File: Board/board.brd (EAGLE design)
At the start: 172.4 x 118.1 mm, 13 parts, among them IC1 L297, IC2 MEGA32-P, J1 +12V

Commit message: Fan, water pump, and supply for motor drive eagle
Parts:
- added C5, C6: 100nF, rcl:C025-025X050
- added C7: 10uF, resistor:E5-10,5
- added D2, D3: 1N5824, diode:DO41-7.6
- added Q1, Q2: BC639, transistor-small-signal:SOT54D
- added R1, R3: (no value), rcl:0207/12
- added R2: 10K, rcl:0207/12
- added S1: (no value), switch-omron:B3F-10XX
- added X1: WATER_PUMP, con-ptr500:AK500/2
- added X2: FAN, con-ptr500:AK500/3
- added X3: STEP_MOT_CD, con-ptr500:AK500/2
- added X4: STEP_MOT_AB, con-ptr500:AK500/2
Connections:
- removed net N$4 (its old number): IC2.9, KANDA.5
- new net N$10: C5.1, IC2.9, KANDA.5, R2.1, S1.1, S1.2
- new net N$11: D3.C, Q2.E, X1.2
- new net N$12: IC2.21, R3.1
- new net N$13: IC1.9, X3.1
- new net N$14: IC1.7, X3.2
- new net N$15: IC1.6, X4.1
- new net N$16: IC1.4, X4.2
- new net N$5: D2.C, Q1.E, X2.3
- new net N$7: Q2.B, R3.2
- new net N$8: Q1.B, R1.2
- new net N$9: IC2.4, R1.1
- new net OLED_RST: IC2.25, OLED_SSD3306_CON.8
- new net OLED_SA: IC2.24, OLED_SSD3306_CON.7
- new net SCL: IC2.22, OLED_SSD3306_CON.5
- new net SDA: IC2.23, OLED_SSD3306_CON.4
- net GND: now also C5.2, C6.2, C7.-, D2.A, D3.A, IC1.11, IC1.13, IC1.14, S1.3, S1.4, X1.1, X2.1
- net VCC: now also C6.1, C7.+, IC1.15, IC1.20, R2.2
- net VSS: now also Q1.C, Q2.C

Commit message: L297 to uC
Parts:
- added CTRL_LED, LED1, LED2, LED3, LED4: (no value), led:LED3MM
- added D10, D11, D4, D5, D6, D7, D8, D9: 1N5819-B, diode:DO41-7.6
- added Q3, Q4, Q5, Q6: BS170, transistor-small-signal:SOT54E
- added R10, R11, R4, R5, R6, R7, R8, R9: 47K, rcl:0207/12
- added R12: 470R, rcl:0207/12
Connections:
- new net N$17: IC1.17, IC2.40
- new net N$18: IC1.18, IC2.39
- new net N$19: IC1.10, IC2.38
- new net N$20: IC1.19, IC2.37
- new net N$21: D4.A, D5.C, Q3.D, R5.1, X4.2
- new net N$22: LED1.K, R5.2
- new net N$23: CTRL_LED.K, R12.2
- new net N$24: D6.A, D7.C, Q4.D, R7.1, X4.1
- new net N$25: LED2.K, R7.2
- new net N$26: CTRL_LED.A, IC2.3
- new net N$27: D8.A, D9.C, Q5.D, R9.1, X3.2
- new net N$28: LED3.K, R9.2
- new net N$29: Q6.G, R10.1
- new net N$30: D10.A, D11.C, Q6.D, R11.1, X3.1
- new net N$31: LED4.K, R11.2
- new net N$32: Q3.G, R4.1
- net GND: now also D11.A, D5.A, D7.A, D9.A, Q3.S, Q4.S, Q5.S, Q6.S, R10.2, R12.1, R4.2, R6.2, R8.2
- net N$13: no longer X3.1
- net N$14: now also Q4.G, R6.1; no longer X3.2
- net N$15: now also Q5.G, R8.1; no longer X4.1
- net N$16: no longer X4.2
- net VCC: now also LED1.A, LED2.A, LED3.A, LED4.A
- net VSS: now also D10.C, D4.C, D6.C, D8.C

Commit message: Signal leds to connectors
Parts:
- added FAN_LED, WP_LED: (no value), led:LED3MM
- added R13, R14: 470R, rcl:0207/12
- R11, R5, R7, R9: value 47K -> 330R
- moved IC1 146.7 mm to (119.4, 22.9), turned to 90 degrees
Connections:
- new net N$33: FAN_LED.A, R13.1
- new net N$34: R14.1, WP_LED.A
- net N$11: now also R14.2
- net N$5: now also R13.2
- net VCC: now also FAN_LED.K, WP_LED.K

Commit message: mcp9808
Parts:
- added C8: 100nF, rcl:C025-025X050
- added U1: MCP9808MSOP, MCP9808:MSOP-8
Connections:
- removed net OLED_RST: IC2.25, OLED_SSD3306_CON.8
- removed net OLED_SA: IC2.24, OLED_SSD3306_CON.7
- removed net SCL: IC2.22, OLED_SSD3306_CON.5
- removed net SDA: IC2.23, OLED_SSD3306_CON.4
- new net N$35: IC2.23, OLED_SSD3306_CON.4, U1.1
- new net N$36: IC2.22, OLED_SSD3306_CON.5, U1.2
- new net N$37: IC2.24, OLED_SSD3306_CON.6
- new net N$38: IC2.25, OLED_SSD3306_CON.7
- new net N$39: IC2.26, OLED_SSD3306_CON.8
- net GND: now also C8.2, U1.4, U1.5, U1.6, U1.7
- net VCC: now also C8.1, U1.8
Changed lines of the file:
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@@
 </element>
 <element name="WP_LED" library="led" library_urn="urn:adsk.eagle:library:259" package="LED3MM" package3d_urn="urn:adsk.eagle:package:15797/1" value="" x="-50.8" y="-836.93"/>
+<element name="U1" library="MCP9808" package="MSOP-8" value="MCP9808MSOP" x="-54.61" y="-847.09">
+<attribute name="AVAILABILITY" value="Good" x="-54.61" y="-847.09" size="1.778" layer="27" display="off"/>
+<attribute name="DESCRIPTION" value=" MCP9808 Series SMD 3.6 V Memory Module Digital Temperature Sensor - MSOP-8 " x="-54.61" y="-847.09" size="1.778" layer="27" display="off"/>
+<attribute name="MF" value="Microchip" x="-54.61" y="-847.09" size="1.778" layer="27" display="off"/>
+<attribute name="MP" value="MCP9808-E/MS" x="-54.61" y="-847.09" size="1.778" layer="27" display="off"/>
+<attribute name="PACKAGE" value="MSOP-8 Microchip" x="-54.61" y="-847.09" size="1.778" layer="27" display="off"/>
+<attribute name="PRICE" value="1.04 USD" x="-54.61" y="-847.09" size="1.778" layer="27" display="off"/>
+</element>
+<element name="C8" library="rcl" library_urn="urn:adsk.eagle:library:334" package="C025-025X050" package3d_urn="urn:adsk.eagle:package:23629/2" value="100nF" x="-50.8" y="-857.25">
+<attribute name="SPICEPREFIX" value="C" x="-50.8" y="-857.25" size="1.778" layer="27" display="off"/>
+</element>
 </elements>
 <signals>
@@
 <contactref element="D11" pad="A"/>
 <contactref element="R12" pad="1"/>
+<contactref element="U1" pad="4"/>
+<contactref element="U1" pad="5"/>
+<contactref element="U1" pad="6"/>
+<contactref element="U1" pad="7"/>
+<contactref element="C8" pad="2"/>
 <wire x1="-49.53" y1="-181.61" x2="-49.53" y2="-195.58" width="0" layer="19" extent="1-1"/>
 <wire x1="-49.53" y1="-167.64" x2="-49.53" y2="-181.61" width="0" layer="19" extent="1-1"/>
@@
 <wire x1="-17.78" y1="18.06" x2="-19.05" y2="10.16" width="0" layer="19" extent="1-1"/>
 <wire x1="-20.78" y1="22.86" x2="-17.78" y2="18.06" width="0" layer="19" extent="1-1"/>
-<wire x1="115.57" y1="29.21" x2="-20.78" y2="22.86" width="0" layer="19" extent="1-1"/>
-<wire x1="115.57" y1="26.67" x2="115.57" y2="29.21" width="0" layer="19" extent="1-1"/>
-<wire x1="115.57" y1="34.29" x2="115.57" y2="29.21" width="0" layer="19" extent="1-1"/>
-<wire x1="123.19" y1="13.97" x2="115.57" y2="26.67" width="0" layer="19" extent="1-1"/>
 <wire x1="-41.91" y1="-320.04" x2="-48.1838" y2="-232.41" width="0" layer="19" extent="1-1"/>
 <wire x1="-43.7388" y1="-354.0506" x2="-41.91" y2="-320.04" width="0" layer="19" extent="1-1"/>
@@
 <wire x1="-24.13" y1="-723.9" x2="-41.91" y2="-723.9" width="0" layer="19" extent="1-1"/>
 <wire x1="-52.07" y1="-781.05" x2="-39.37" y2="-739.14" width="0" layer="19" extent="1-1"/>
+<wire x1="-52.41" y1="-846.765" x2="-52.07" y2="-781.05" width="0" layer="19" extent="1-1"/>
+<wire x1="-52.41" y1="-847.415" x2="-52.41" y2="-846.765" width="0" layer="19" extent="1-1"/>
+<wire x1="-52.41" y1="-848.065" x2="-52.41" y2="-847.415" width="0" layer="19" extent="1-1"/>
+<wire x1="-56.81" y1="-848.065" x2="-52.41" y2="-848.065" width="0" layer="19" extent="1-1"/>
+<wire x1="-49.53" y1="-857.25" x2="-52.41" y2="-848.065" width="0" layer="19" extent="1-1"/>
+<wire x1="115.57" y1="26.67" x2="-15.6464" y2="1.8288" width="0" layer="19" extent="1-1"/>
+<wire x1="115.57" y1="29.21" x2="115.57" y2="26.67" width="0" layer="19" extent="1-1"/>
+<wire x1="115.57" y1="34.29" x2="115.57" y2="29.21" width="0" layer="19" extent="1-1"/>
+<wire x1="123.19" y1="13.97" x2="115.57" y2="26.67" width="0" layer="19" extent="1-1"/>
 </signal>
 <signal name="VCC">
@@
 <contactref element="FAN_LED" pad="K"/>
 <contactref element="WP_LED" pad="K"/>
+<contactref element="U1" pad="8"/>
+<contactref element="C8" pad="1"/>
 <wire x1="-52.07" y1="-181.61" x2="-52.07" y2="-195.58" width="0" layer="19" extent="1-1"/>
 <wire x1="-52.07" y1="-167.64" x2="-52.07" y2="-181.61" width="0" layer="19" extent="1-1"/>
@@
 <wire x1="-49.53" y1="-808.99" x2="-25.4" y2="-753.11" width="0" layer="19" extent="1-1"/>
 <wire x1="-49.53" y1="-836.93" x2="-49.53" y2="-808.99" width="0" layer="19" extent="1-1"/>
+<wire x1="-52.41" y1="-846.115" x2="-49.53" y2="-836.93" width="0" layer="19" extent="1-1"/>
+<wire x1="-52.07" y1="-857.25" x2="-52.41" y2="-846.115" width="0" layer="19" extent="1-1"/>
 </signal>
 <signal name="N$1">
@@
 <wire x1="-36.83" y1="-137.16" x2="-40.64" y2="-153.67" width="0" layer="19" extent="1-1"/>
 </signal>
-<signal name="SDA">
-<contactref element="IC2" pad="23"/>
-<contactref element="OLED_SSD3306_CON" pad="4"/>
-<wire x1="-8.89" y1="-121.92" x2="-44.45" y2="-195.58" width="0" layer="19" extent="1-1"/>
-</signal>
-<signal name="SCL">
-<contactref element="OLED_SSD3306_CON" pad="5"/>
-<contactref element="IC2" pad="22"/>
-<wire x1="-6.35" y1="-121.92" x2="-41.91" y2="-195.58" width="0" layer="19" extent="1-1"/>
-</signal>
-<signal name="OLED_RST">
-<contactref element="OLED_SSD3306_CON" pad="8"/>
-<contactref element="IC2" pad="25"/>
-<wire x1="-13.97" y1="-121.92" x2="-34.29" y2="-195.58" width="0" layer="19" extent="1-1"/>
-</signal>
-<signal name="OLED_SA">
-<contactref element="OLED_SSD3306_CON" pad="7"/>
-<contactref element="IC2" pad="24"/>
-<wire x1="-11.43" y1="-121.92" x2="-36.83" y2="-195.58" width="0" layer="19" extent="1-1"/>
-</signal>
 <signal name="N$3">
 <contactref element="KANDA" pad="1"/>
@@
 <wire x1="-52.07" y1="-822.96" x2="-52.07" y2="-836.93" width="0" layer="19" extent="1-1"/>
 </signal>
+<signal name="N$35">
+<contactref element="IC2" pad="23"/>
+<contactref element="OLED_SSD3306_CON" pad="4"/>
+<contactref element="U1" pad="1"/>
+<wire x1="-8.89" y1="-121.92" x2="-44.45" y2="-195.58" width="0" layer="19" extent="1-1"/>
+<wire x1="-56.81" y1="-846.115" x2="-44.45" y2="-195.58" width="0" layer="19" extent="1-1"/>
+</signal>
+<signal name="N$36">
+<contactref element="IC2" pad="22"/>
+<contactref element="OLED_SSD3306_CON" pad="5"/>
+<contactref element="U1" pad="2"/>
+<wire x1="-6.35" y1="-121.92" x2="-41.91" y2="-195.58" width="0" layer="19" extent="1-1"/>
+<wire x1="-56.81" y1="-846.765" x2="-41.91" y2="-195.58" width="0" layer="19" extent="1-1"/>
+</signal>
+<signal name="N$37">
+<contactref element="IC2" pad="24"/>
+<contactref element="OLED_SSD3306_CON" pad="6"/>
+<wire x1="-11.43" y1="-121.92" x2="-39.37" y2="-195.58" width="0" layer="19" extent="1-1"/>
+</signal>
+<signal name="N$38">
+<contactref element="OLED_SSD3306_CON" pad="7"/>
+<contactref element="IC2" pad="25"/>
+<wire x1="-13.97" y1="-121.92" x2="-36.83" y2="-195.58" width="0" layer="19" extent="1-1"/>
+</signal>
+<signal name="N$39">
+<contactref element="IC2" pad="26"/>
+<contactref element="OLED_SSD3306_CON" pad="8"/>
+<wire x1="-16.51" y1="-121.92" x2="-34.29" y2="-195.58" width="0" layer="19" extent="1-1"/>
+</signal>
 </signals>

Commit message: stepper motor l298
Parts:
- removed D11: 1N5819-B, diode:DO41-7.6
- removed LED1, LED2, LED3, LED4: (no value), led:LED3MM
- removed Q2: BC639, transistor-small-signal:SOT54D
- removed Q4, Q5, Q6: BS170, transistor-small-signal:SOT54E
- removed R10, R6, R8: 47K, rcl:0207/12
- removed R11, R9: 330R, rcl:0207/12
- removed R13, R14: 470R, rcl:0207/12
- removed R3: (no value), rcl:0207/12
- removed X3: STEP_MOT_CD, con-ptr500:AK500/2
- removed X4: STEP_MOT_AB, con-ptr500:AK500/2
- added IC3: L298, st-microelectronics:MULTIWATT-15
- added X5: STEP_MOT_CD, con-ptr500:AK500/2
- added X6: STEP_MOT_AB, con-ptr500:AK500/2
- D10, D4, D5, D6, D7, D8, D9: value 1N5819-B -> 1N5824
- Q3: value BS170 -> BC639; device transistor-small-signal:SOT54E -> transistor-small-signal:SOT54D
- R4: value 47K -> 470R
- R5: value 330R -> (none)
- R7: value 330R -> 470R
- moved D2 600.3 mm to (-96.5, -918.2)
- moved D3 527.0 mm to (-96.5, -957.6)
- moved D4 448.7 mm to (-96.5, -965.2)
- moved D5 438.6 mm to (-96.5, -972.8)
- moved Q3 438.3 mm to (-99.1, -925.8)
- moved R4 411.8 mm to (-94.0, -913.1)
- moved D6 402.0 mm to (-96.5, -980.4)
- moved R5 392.9 mm to (-94.0, -942.3)
- moved D7 391.9 mm to (-96.5, -988.1)
- moved D8 355.4 mm to (-96.5, -995.7)
- moved D9 345.4 mm to (-96.5, -1003.3)
- moved R7 327.4 mm to (-94.0, -952.5)
- moved D10 309.0 mm to (-96.5, -1010.9)
- moved IC1 215.9 mm to (-96.5, 26.7)
- moved L1 163.8 mm to (48.3, 50.8)
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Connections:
- removed net N$11: D3.C, Q2.E, R14.2, X1.2
- removed net N$14: IC1.7, Q4.G, R6.1
- removed net N$22: LED1.K, R5.2
- removed net N$24: D6.A, D7.C, Q4.D, R7.1, X4.1
- removed net N$25: LED2.K, R7.2
- removed net N$30: D10.A, D11.C, Q6.D, R11.1, X3.1
- removed net N$31: LED4.K, R11.2
- removed net N$32: Q3.G, R4.1
- removed net N$34: R14.1, WP_LED.A
- removed net N$5 (its old number): D2.C, Q1.E, R13.2, X2.3
- removed net N$7: Q2.B, R3.2
- new net N$56: IC1.7, IC3.7
- new net N$58: IC1.6, IC3.10
- new net N$9: Q1.C, X2.1
- new net VSS1: D10.C, D3.A, D4.A, D5.A, D6.A, D7.C, D8.C, D9.C, IC3.13, IC3.14, IC3.2, IC3.3, X5.1, X5.2, X6.1, X6.2
- net GND: now also D10.A, D8.A, FAN_LED.A, IC3.1, IC3.15, IC3.8, Q1.E, Q3.E, R4.1, R7.1, WP_LED.A; no longer D11.A, D2.A, D3.A, D5.A, Q3.S, Q4.S, Q5.S, Q6.S, R10.2, R4.2, R6.2, R8.2, X1.1, X2.1
- net N$12: now also R5.1; no longer R3.1
- net N$13: now also IC3.5
- net N$15: now also IC1.5, IC3.6; no longer IC1.6, Q5.G, R8.1
- net N$16: now also IC3.12
- net N$21: now also IC1.8, IC3.11; no longer D4.A, D5.C, Q3.D, R5.1, X4.2
- net N$27: now also FAN_LED.K, R4.2; no longer D8.A, D9.C, Q5.D, R9.1, X3.2
- net N$28: now also Q3.B, R5.2; no longer LED3.K, R9.2
- net N$29: now also D2.A, Q3.C, X1.1; no longer Q6.G, R10.1
- net N$33: now also R7.2, WP_LED.K; no longer FAN_LED.A, R13.1
- net VCC: now also IC3.9; no longer FAN_LED.K, LED1.A, LED2.A, LED3.A, LED4.A, WP_LED.K
- net VSS: now also D2.C, D3.C, D5.C, IC3.4, X1.2, X2.3; no longer D10.C, D8.C, Q1.C, Q2.C
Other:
- board size 172.4 x 118.1 mm -> 242.2 x 185.4 mm

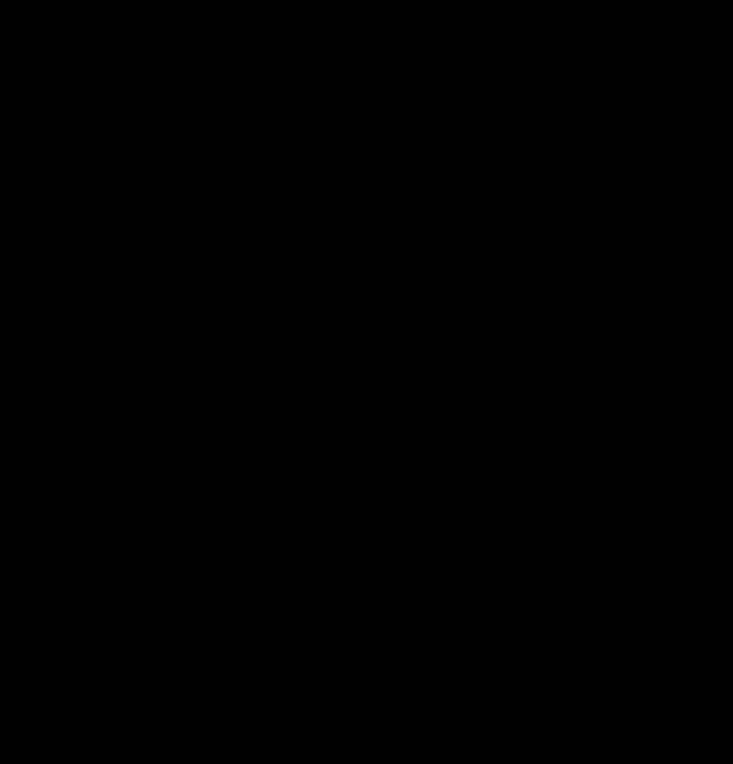
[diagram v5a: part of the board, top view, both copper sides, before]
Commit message: added filter for vss l298
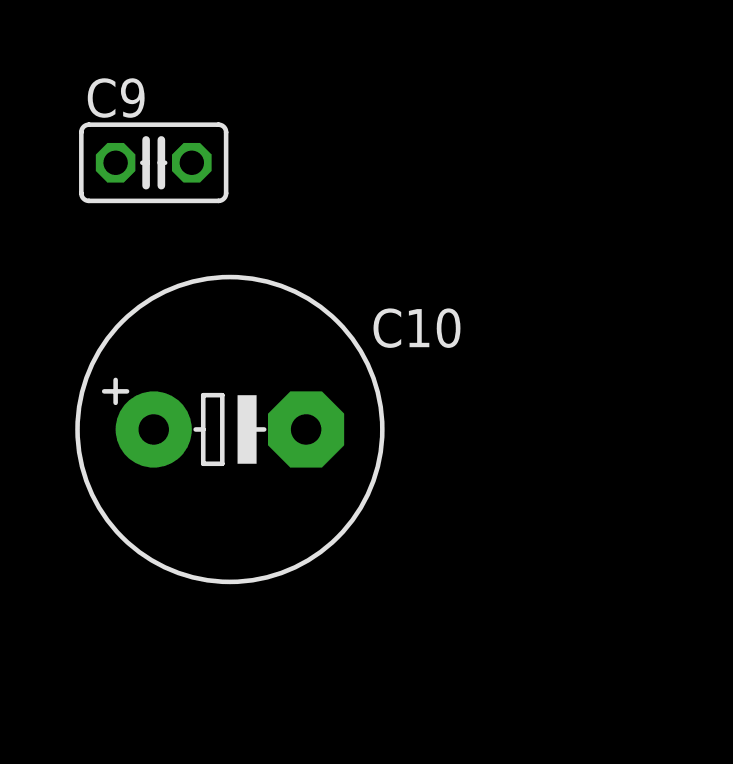
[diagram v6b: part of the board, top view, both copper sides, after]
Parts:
- added C10: 22uF, resistor:E5-10,5
- added C9: 100nF, rcl:C025-025X050
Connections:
- net GND: now also C10.-, C9.2
- net VSS: now also C10.+, C9.1
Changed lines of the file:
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@@
 <element name="D9" library="diode" package="DO41-7.6" value="1N5824" x="-96.52" y="-1003.3"/>
 <element name="D10" library="diode" package="DO41-7.6" value="1N5824" x="-96.52" y="-1010.92"/>
+<element name="C9" library="rcl" package="C025-025X050" value="100nF" x="-99.06" y="82.55">
+<attribute name="SPICEPREFIX" value="C" x="-99.06" y="-1018.54" size="1.778" layer="27" display="off"/>
+</element>
+<element name="C10" library="resistor" package="E5-10,5" value="22uF" x="-96.52" y="73.66"/>
 </elements>
 <signals>
@@
 <contactref element="D9" pad="A"/>
 <contactref element="D10" pad="A"/>
+<contactref element="C10" pad="-"/>
+<contactref element="C9" pad="2"/>
 <wire x1="-100.33" y1="-906.78" x2="-100.33" y2="-913.13" width="0" layer="19" extent="1-1"/>
 <wire x1="-100.33" y1="-925.83" x2="-100.33" y2="-913.13" width="0" layer="19" extent="1-1"/>
@@
 <wire x1="-100.33" y1="33.02" x2="-100.33" y2="30.48" width="0" layer="19" extent="1-1"/>
 <wire x1="-100.33" y1="38.1" x2="-100.33" y2="33.02" width="0" layer="19" extent="1-1"/>
-<wire x1="-0.46" y1="52.07" x2="-92.71" y2="17.78" width="0" layer="19" extent="1-1"/>
+<wire x1="-93.98" y1="73.66" x2="-100.33" y2="38.1" width="0" layer="19" extent="1-1"/>
+<wire x1="-97.79" y1="82.55" x2="-93.98" y2="73.66" width="0" layer="19" extent="1-1"/>
+<wire x1="-0.46" y1="52.07" x2="-93.98" y2="73.66" width="0" layer="19" extent="1-1"/>
 <wire x1="2.54" y1="47.27" x2="-0.46" y2="52.07" width="0" layer="19" extent="1-1"/>
 <wire x1="31.75" y1="53.8988" x2="2.54" y2="47.27" width="0" layer="19" extent="1-1"/>
@@
 <contactref element="D5" pad="C"/>
 <contactref element="D6" pad="C"/>
+<contactref element="C9" pad="1"/>
+<contactref element="C10" pad="+"/>
 <wire x1="-100.33" y1="-918.21" x2="-96.52" y2="-866.14" width="0" layer="19" extent="1-1"/>
 <wire x1="-100.33" y1="-957.58" x2="-100.33" y2="-918.21" width="0" layer="19" extent="1-1"/>
@@
 <wire x1="17.78" y1="53.34" x2="-31.75" y2="-58.42" width="0" layer="19" extent="1-1"/>
 <wire x1="28.3464" y1="53.8988" x2="17.78" y2="53.34" width="0" layer="19" extent="1-1"/>
+<wire x1="-99.06" y1="73.66" x2="17.78" y2="53.34" width="0" layer="19" extent="1-1"/>
+<wire x1="-100.33" y1="82.55" x2="-99.06" y2="73.66" width="0" layer="19" extent="1-1"/>
 </signal>
 <signal name="N$2">

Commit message: Added pcb design #1
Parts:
- added C11: 100nF, rcl:C025-025X050
- added R3: 470R, rcl:0207/12
- added VSS_LED: (no value), led:LED3MM
- CTRL_LED, FAN_LED, WP_LED: device led:LED3MM -> led:LED5MM
- R12: value 470R -> 330R
- X5: value STEP_MOT_CD -> SM_CD
- X6: value STEP_MOT_AB -> SM_AB
- moved D10 928.1 mm to (75.5, -98.9), turned to 270 degrees
- moved D9 919.1 mm to (69.5, -99.3), turned to 270 degrees
- moved D6 910.4 mm to (75.5, -86.4), turned to 270 degrees
- moved D8 910.2 mm to (63.5, -99.7), turned to 270 degrees
- moved D5 901.4 mm to (69.5, -86.8), turned to 270 degrees
- moved D7 901.3 mm to (57.5, -100.1), turned to 270 degrees
- moved D4 892.5 mm to (63.5, -87.2), turned to 270 degrees
- moved R5 886.4 mm to (93.7, -76.0), turned to 270 degrees
- moved D3 883.5 mm to (57.5, -87.6), turned to 270 degrees
- moved R7 873.0 mm to (16.0, -86.5)
- moved Q3 857.8 mm to (92.9, -89.8)
- moved WP_LED 855.5 mm to (-2.00, -86.0)
- moved D2 828.4 mm to (104.2, -114.5), turned to 270 degrees
- moved R4 827.3 mm to (16.0, -93.1), turned to 1.1 degrees
- moved FAN_LED 818.6 mm to (-2.00, -94.0)
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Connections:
- removed net N$27: FAN_LED.K, R4.2
- removed net N$33: R7.2, WP_LED.K
- new net N$11: IC2.27, R12.2
- new net N$14: CTRL_LED.A, R12.1
- new net N$22: R7.1, WP_LED.A
- new net N$24: D5.A, D9.C, IC3.13, X5.2
- new net N$7: R3.2, VSS_LED.K
- net GND: now also C11.2, CTRL_LED.K, FAN_LED.K, R3.1, R4.2, R7.2, WP_LED.K; no longer FAN_LED.A, R12.1, R4.1, R7.1, WP_LED.A
- net N$23: now also FAN_LED.A, R4.1; no longer CTRL_LED.K, R12.2
- net N$26: no longer CTRL_LED.A
- net VCC: now also C11.1
- net VSS: now also VSS_LED.A
- net VSS1: no longer D5.A, D9.C, IC3.13, X5.2
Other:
- board size 242.2 x 185.4 mm -> 135 x 99.4 mm

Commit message: auto route
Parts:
- VSS_LED: device led:LED3MM -> led:LED5MM
- moved R3 64.0 mm to (16.0, -106.0)
- moved VSS_LED 64.0 mm to (-2.00, -112.0)
- moved S1 13.2 mm to (13.0, -114.2), turned to 180 degrees
- moved C5 12.6 mm to (20.3, -114.8), turned to 90 degrees
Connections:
- net GND: now also VSS_LED.K; no longer R3.1
- net N$7: now also R3.1, VSS_LED.A; no longer R3.2, VSS_LED.K
- net VSS: now also R3.2; no longer VSS_LED.A
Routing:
- net GND: track 0.00 -> 486.9 mm, vias 0 -> 1
- net VCC: track 0.00 -> 260.9 mm, vias 0 -> 2
- net VSS: track 0.00 -> 225.3 mm, vias 0 -> 1
- net N$10: track 0.00 -> 165.6 mm
- net N$36: track 0.00 -> 146.4 mm
- net N$35: track 0.00 -> 132.1 mm
- net N$11: track 0.00 -> 117.3 mm
- net N$37: track 0.00 -> 113.7 mm
- net N$38: track 0.00 -> 106.3 mm
- net VSS1: track 0.00 -> 105.5 mm
- net N$39: track 0.00 -> 97.9 mm
- net N$24: track 0.00 -> 55.2 mm
- net N$13: track 0.00 -> 54.3 mm
- net N$56: track 0.00 -> 48.0 mm
- net N$21: track 0.00 -> 46.3 mm
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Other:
- board size 135 x 99.4 mm -> 131 x 95.4 mm
